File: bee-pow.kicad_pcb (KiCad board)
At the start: 2 copper layers, 29 x 53.3 mm, 48 parts, among them J1 Conn_01x02_Male, J2 Conn_01x02_Male, J3 Conn_01x02_Male, J4 Conn_01x02_Male, J5 Screw_Terminal_01x04, U1 L7805, U2 L7815, U3 L7915

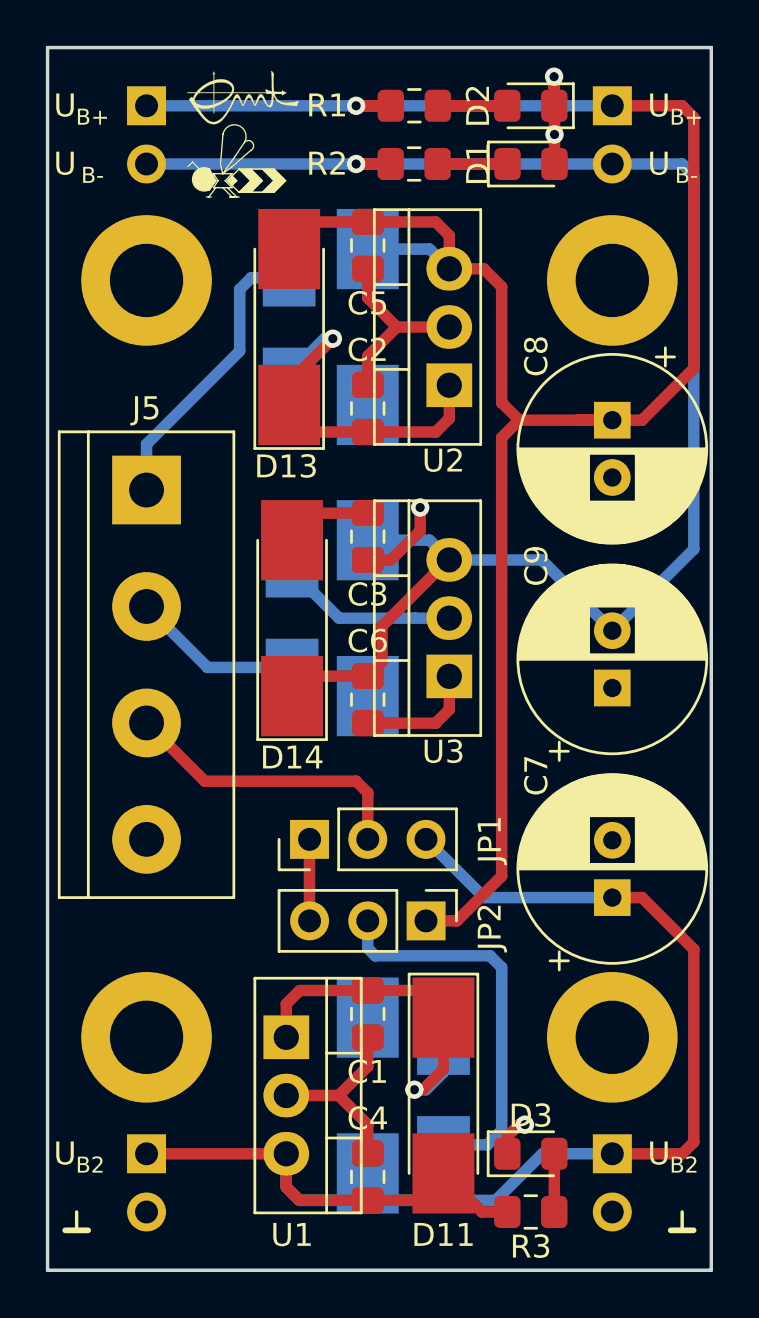
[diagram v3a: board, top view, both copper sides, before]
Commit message: DRC - add missing via, fix part distances.
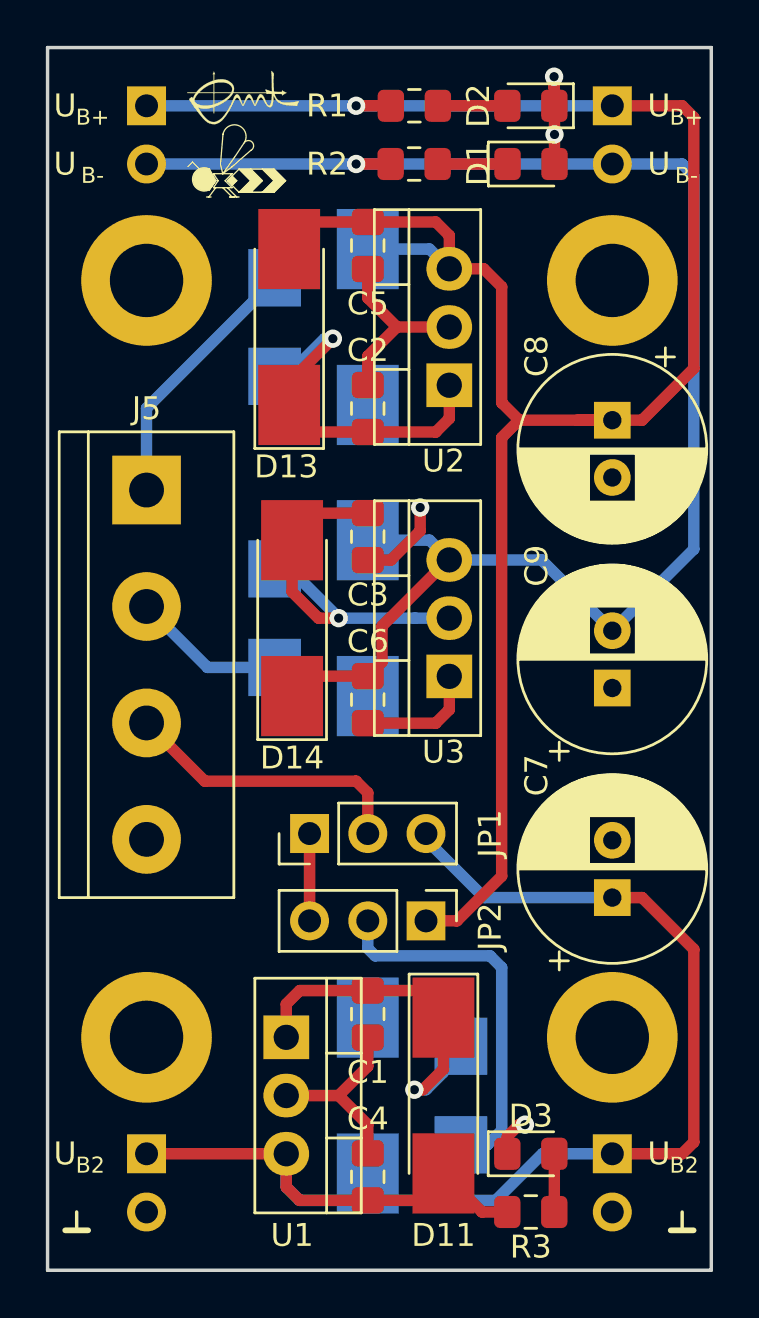
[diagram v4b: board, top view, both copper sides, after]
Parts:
- moved D9 0.76 mm to (92.5, 134.6)
- moved D6 0.76 mm to (84.3, 113.8)
- moved D5 0.63 mm to (84.3, 101.1)
- moved JP1 0.25 mm to (85.9, 123.2)
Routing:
- net Net-(C3-Pad2): track 11.6 -> 16.4 mm, vias 0 -> 1
- net U1: track 12.8 -> 11.6 mm
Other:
- net class Default: trace_width 0.25 -> 0.5
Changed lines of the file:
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@@
     (thickness 1.6)
     (drawings 5)
-    (tracks 155)
+    (tracks 157)
     (zones 0)
     (modules 48)
@@
     (0 F.Cu signal)
     (31 B.Cu signal)
-    (32 B.Adhes user)
+    (32 B.Adhes user hide)
     (33 F.Adhes user)
-    (34 B.Paste user)
+    (34 B.Paste user hide)
     (35 F.Paste user)
-    (36 B.SilkS user)
+    (36 B.SilkS user hide)
     (37 F.SilkS user)
-    (38 B.Mask user)
+    (38 B.Mask user hide)
     (39 F.Mask user)
     (40 Dwgs.User user)
@@
     (44 Edge.Cuts user)
     (45 Margin user)
-    (46 B.CrtYd user)
+    (46 B.CrtYd user hide)
     (47 F.CrtYd user)
     (48 B.Fab user hide)
@@
   )
   (setup
-    (last_trace_width 0.25)
+    (last_trace_width 0.5)
     (user_trace_width 0.5)
     (trace_clearance 0.2)
@@
   (net_class Default "Dies ist die voreingestellte Netzklasse."
     (clearance 0.2)
-    (trace_width 0.25)
+    (trace_width 0.5)
     (via_dia 0.8)
     (via_drill 0.4)
@@
   )
   (module Connector_PinHeader_2.54mm:PinHeader_1x03_P2.54mm_Vertical (layer F.Cu)
-    (at 85.852 123.444 90)
+    (at 85.852 123.19 90)
     (descr "Through hole straight pin header, 1x03, 2.54mm pitch, single row")
     (tags "Through hole pin header THT 1x03 2.54mm single row")
@@
   )
   (module Diode_SMD:D_SMB (layer B.Cu)
-    (at 84.963 101.092 90)
+    (at 84.328 101.092 90)
     (descr "Diode SMB (DO-214AA)")
     (tags "Diode SMB (DO-214AA)")
@@
   )
   (module Diode_SMD:D_SMB (layer B.Cu)
-    (at 91.694 134.62 270)
+    (at 92.456 134.62 270)
     (descr "Diode SMB (DO-214AA)")
     (tags "Diode SMB (DO-214AA)")
@@
   )
   (module Diode_SMD:D_SMB (layer B.Cu)
-    (at 85.089999 113.792 90)
+    (at 84.328 113.792 90)
     (descr "Diode SMB (DO-214AA)")
     (tags "Diode SMB (DO-214AA)")
@@
   (segment (start 96.52 90.17) (end 96.52 90.17) (width 0.5) (layer F.Cu) (net 1))
   (via (at 96.52 90.17) (size 0.8) (drill 0.4) (layers F.Cu B.Cu) (net 1))
-  (segment (start 83.313 98.942) (end 84.963 98.942) (width 0.5) (layer B.Cu) (net 2))
-  (segment (start 82.804 99.451) (end 83.313 98.942) (width 0.5) (layer B.Cu) (net 2))
-  (segment (start 82.804 102.14) (end 82.804 99.451) (width 0.5) (layer B.Cu) (net 2))
-  (segment (start 78.74 106.204) (end 82.804 102.14) (width 0.5) (layer B.Cu) (net 2))
-  (segment (start 78.74 108.204) (end 78.74 106.204) (width 0.5) (layer B.Cu) (net 2))
+  (segment (start 84.328 99.042) (end 84.328 98.942) (width 0.5) (layer B.Cu) (net 2))
+  (segment (start 78.74 104.63) (end 84.328 99.042) (width 0.5) (layer B.Cu) (net 2))
+  (segment (start 78.74 108.204) (end 78.74 104.63) (width 0.5) (layer B.Cu) (net 2))
   (segment (start 81.398 115.942) (end 85.089999 115.942) (width 0.5) (layer B.Cu) (net 3))
   (segment (start 78.74 113.284) (end 81.398 115.942) (width 0.5) (layer B.Cu) (net 3))
@@
   (segment (start 94.234 125.048) (end 94.234 105.918) (width 0.5) (layer F.Cu) (net 8))
   (segment (start 94.479 91.44) (end 91.449 91.44) (width 0.5) (layer F.Cu) (net 9))
-  (segment (start 86.270999 109.211) (end 85.089999 110.392) (width 0.5) (layer F.Cu) (net 10))
-  (segment (start 88.392 109.211) (end 86.270999 109.211) (width 0.5) (layer F.Cu) (net 10))
   (segment (start 90.448 113.792) (end 91.948 113.792) (width 0.5) (layer B.Cu) (net 10))
   (segment (start 87.139999 113.792) (end 90.448 113.792) (width 0.5) (layer B.Cu) (net 10))
   (segment (start 85.089999 111.742) (end 87.139999 113.792) (width 0.5) (layer B.Cu) (net 10))
   (segment (start 85.089999 111.642) (end 85.089999 111.742) (width 0.5) (layer B.Cu) (net 10))
+  (segment (start 86.270999 109.211) (end 85.089999 110.392) (width 0.5) (layer F.Cu) (net 10))
+  (segment (start 88.392 109.211) (end 86.270999 109.211) (width 0.5) (layer F.Cu) (net 10))
+  (segment (start 85.089999 112.642) (end 86.239999 113.792) (width 0.5) (layer F.Cu) (net 10))
+  (segment (start 85.089999 110.392) (end 85.089999 112.642) (width 0.5) (layer F.Cu) (net 10))
+  (segment (start 86.239999 113.792) (end 87.122 113.792) (width 0.5) (layer F.Cu) (net 10))
+  (via (at 87.122 113.792) (size 0.8) (drill 0.4) (layers F.Cu B.Cu) (net 10))
   (segment (start 86.144 105.673) (end 84.963 104.492) (width 0.5) (layer F.Cu) (net 11))
   (segment (start 88.392 105.673) (end 86.144 105.673) (width 0.5) (layer F.Cu) (net 11))
